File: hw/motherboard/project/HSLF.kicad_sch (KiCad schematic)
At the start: 41 parts, among them SW1 SW_Push, SW2 SW_Push, U1 STM32F103C8T6, U2 TPS563201, U3 AMS1117-5.0, Y1 12MHz, Y2 DNP 32.768k

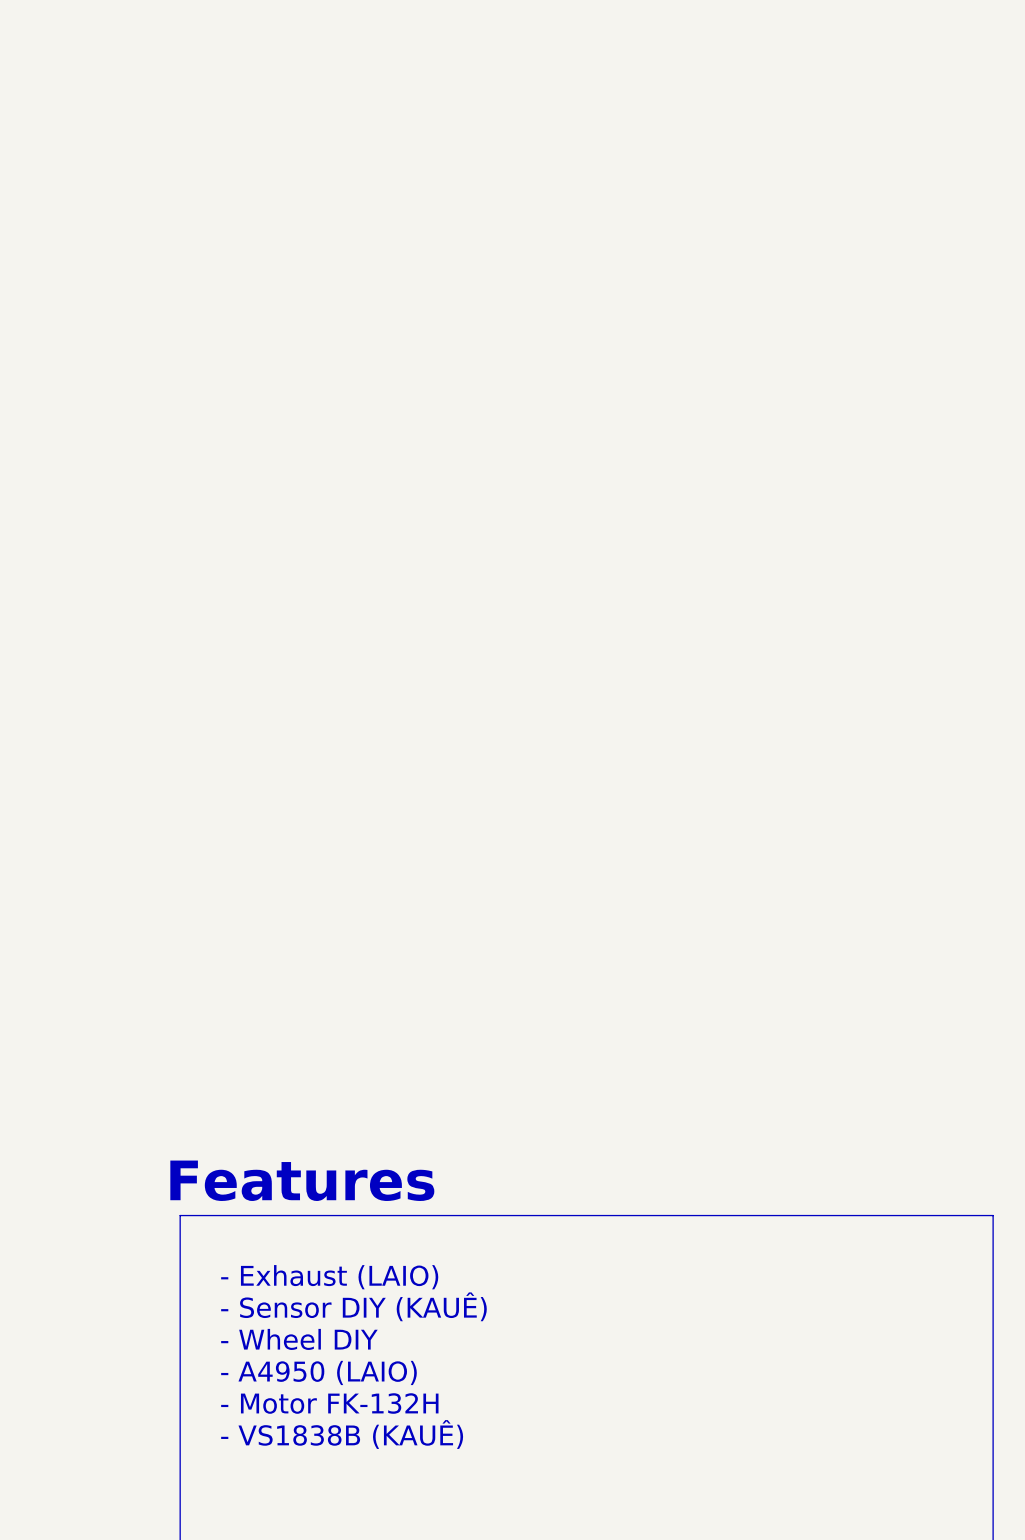
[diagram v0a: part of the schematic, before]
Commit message: Add Features and Sugestions, add sensors-array project
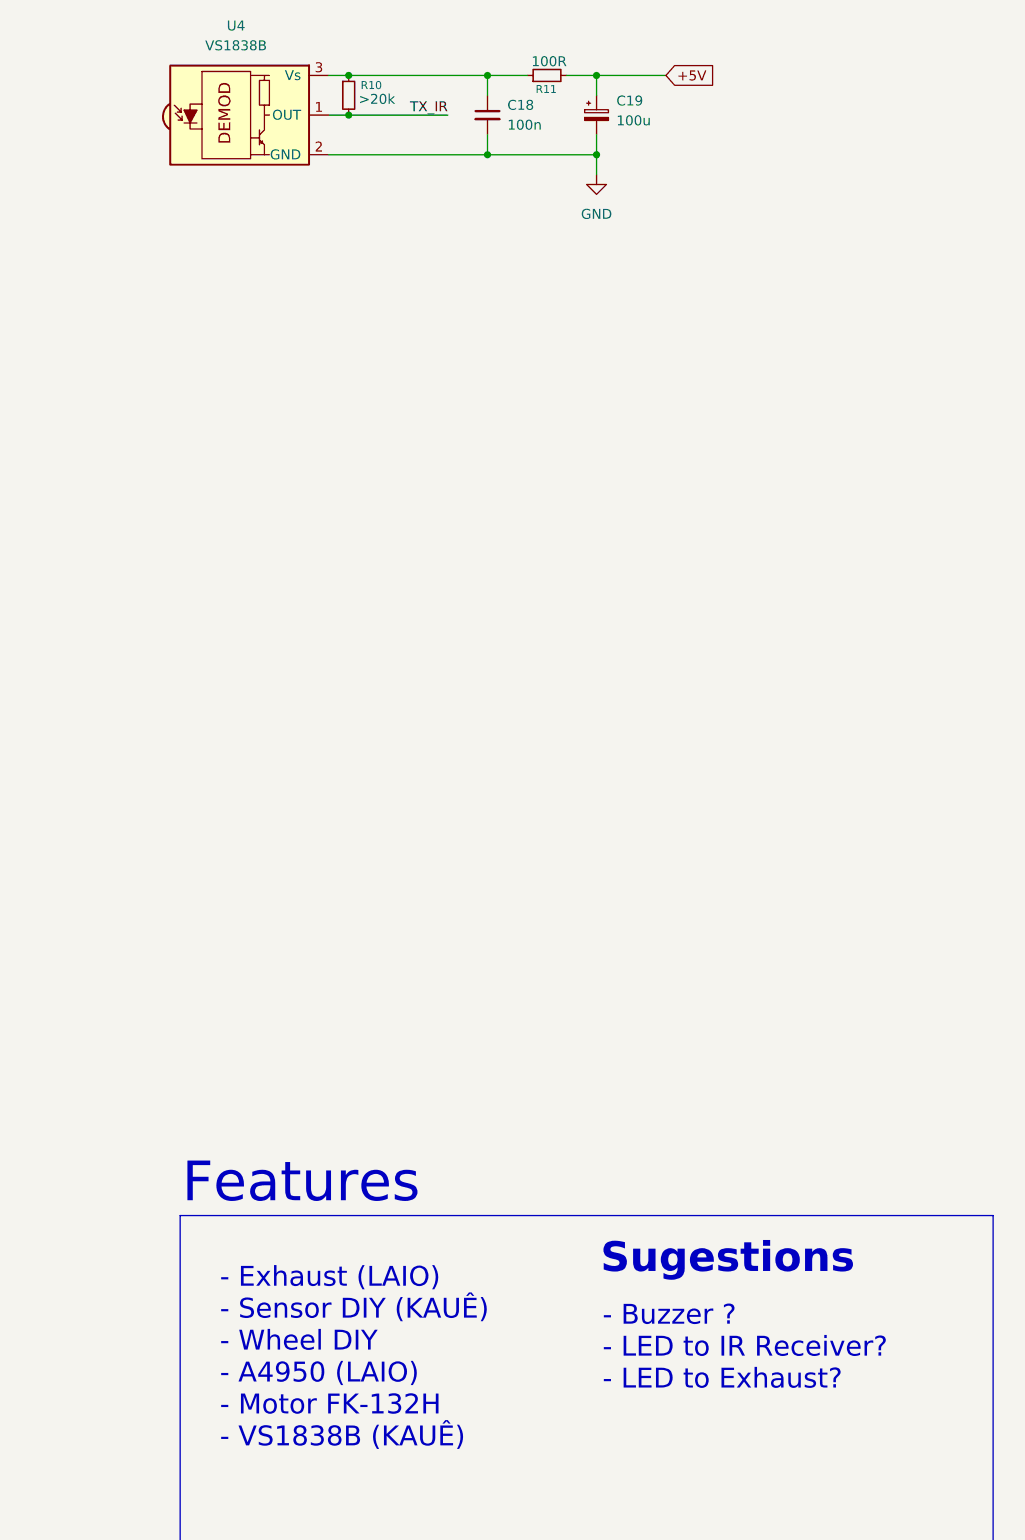
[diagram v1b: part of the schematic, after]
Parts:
- added C18: 100n, symbol Device:C_Small
- added C19: 100u, symbol Device:C_Polarized_Small
- added R10: >20k, symbol Device:R_Small
- added R11: 100R, symbol Device:R_Small
- added U4: VS1838B, OptoDevice:Vishay_MOLD-3Pin, symbol Interface_Optical:TSDP341xx
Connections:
- net +5V: now also C19.1, R11.2
- net GND: now also C18.2, C19.2, U4.2 (GND)
- new net: C18.1, R10.1, R11.1, U4.3 (Vs)
- new net TX_IR: R10.2, U4.1 (OUT)
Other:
- note added: "- Buzzer ? - LED to IR Receiver? - LED to Exhaust?"
- note added: "Sugestions"

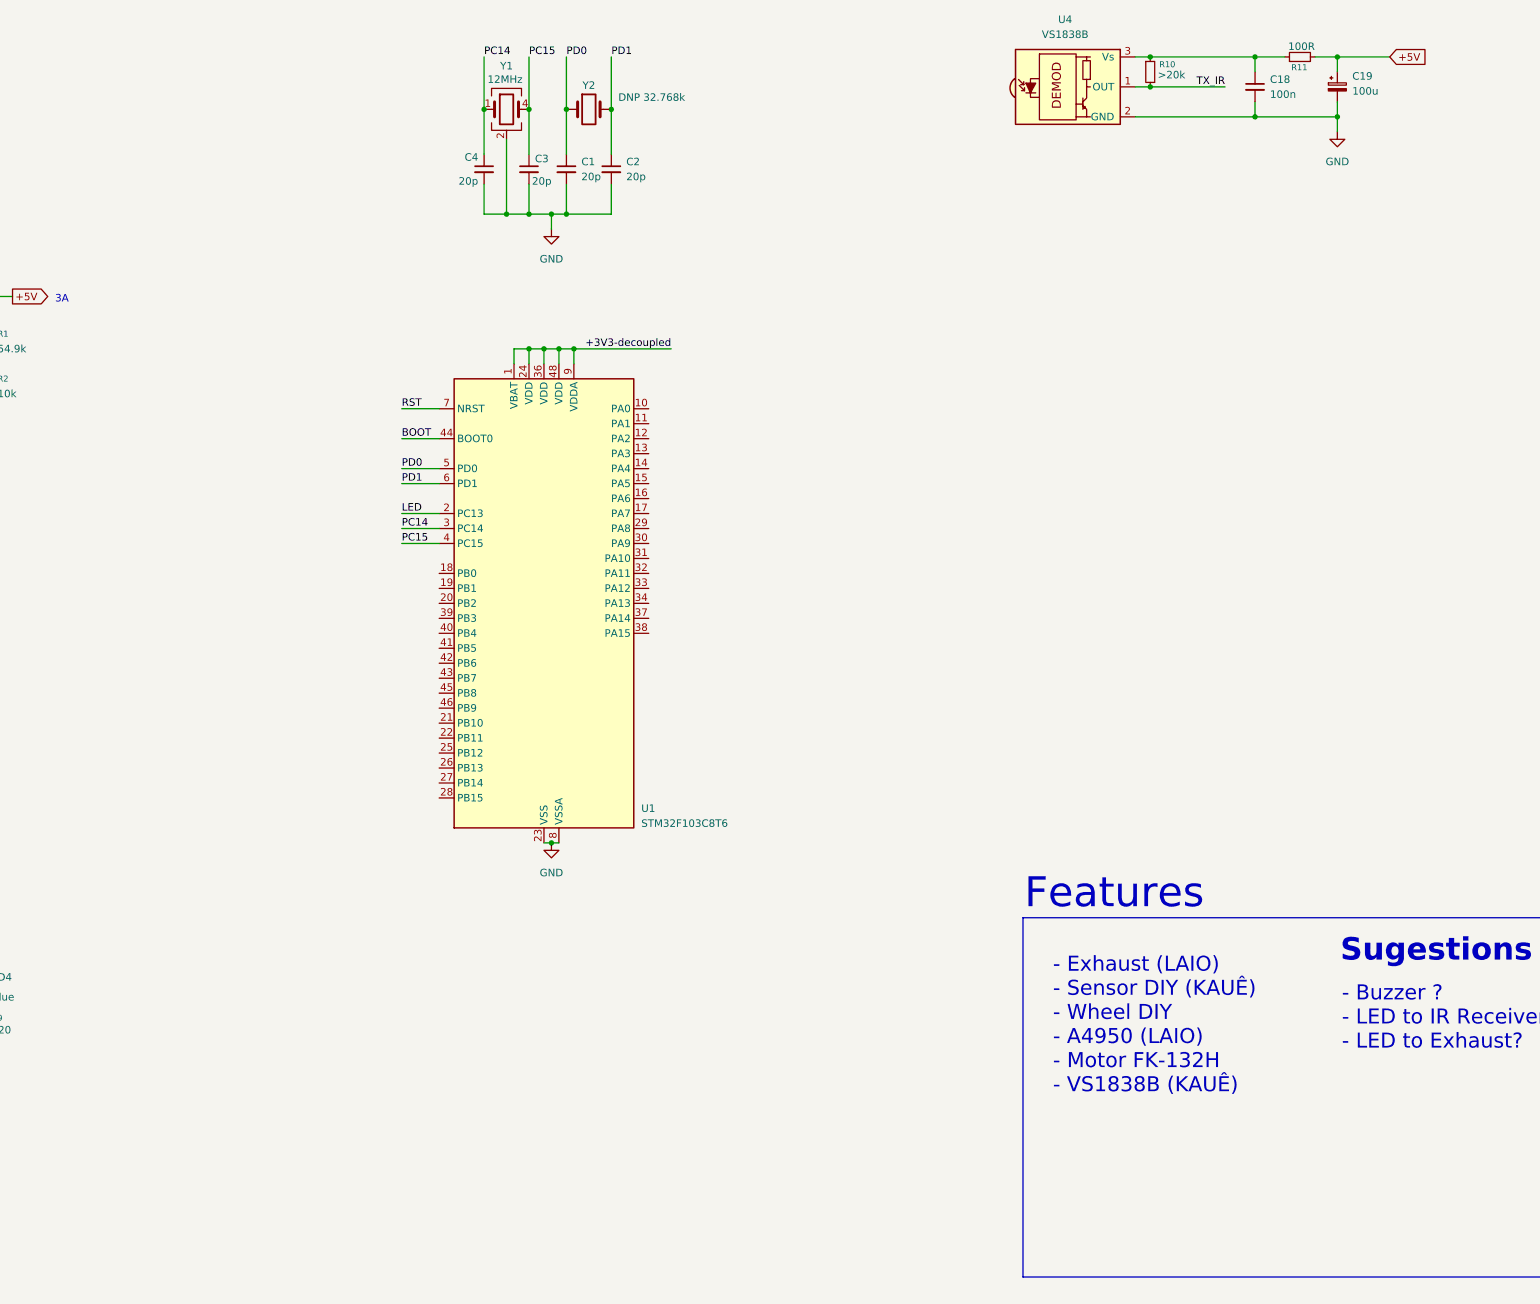
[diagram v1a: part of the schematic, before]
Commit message: criacao do driver do exaustor e driver para motores de tracao
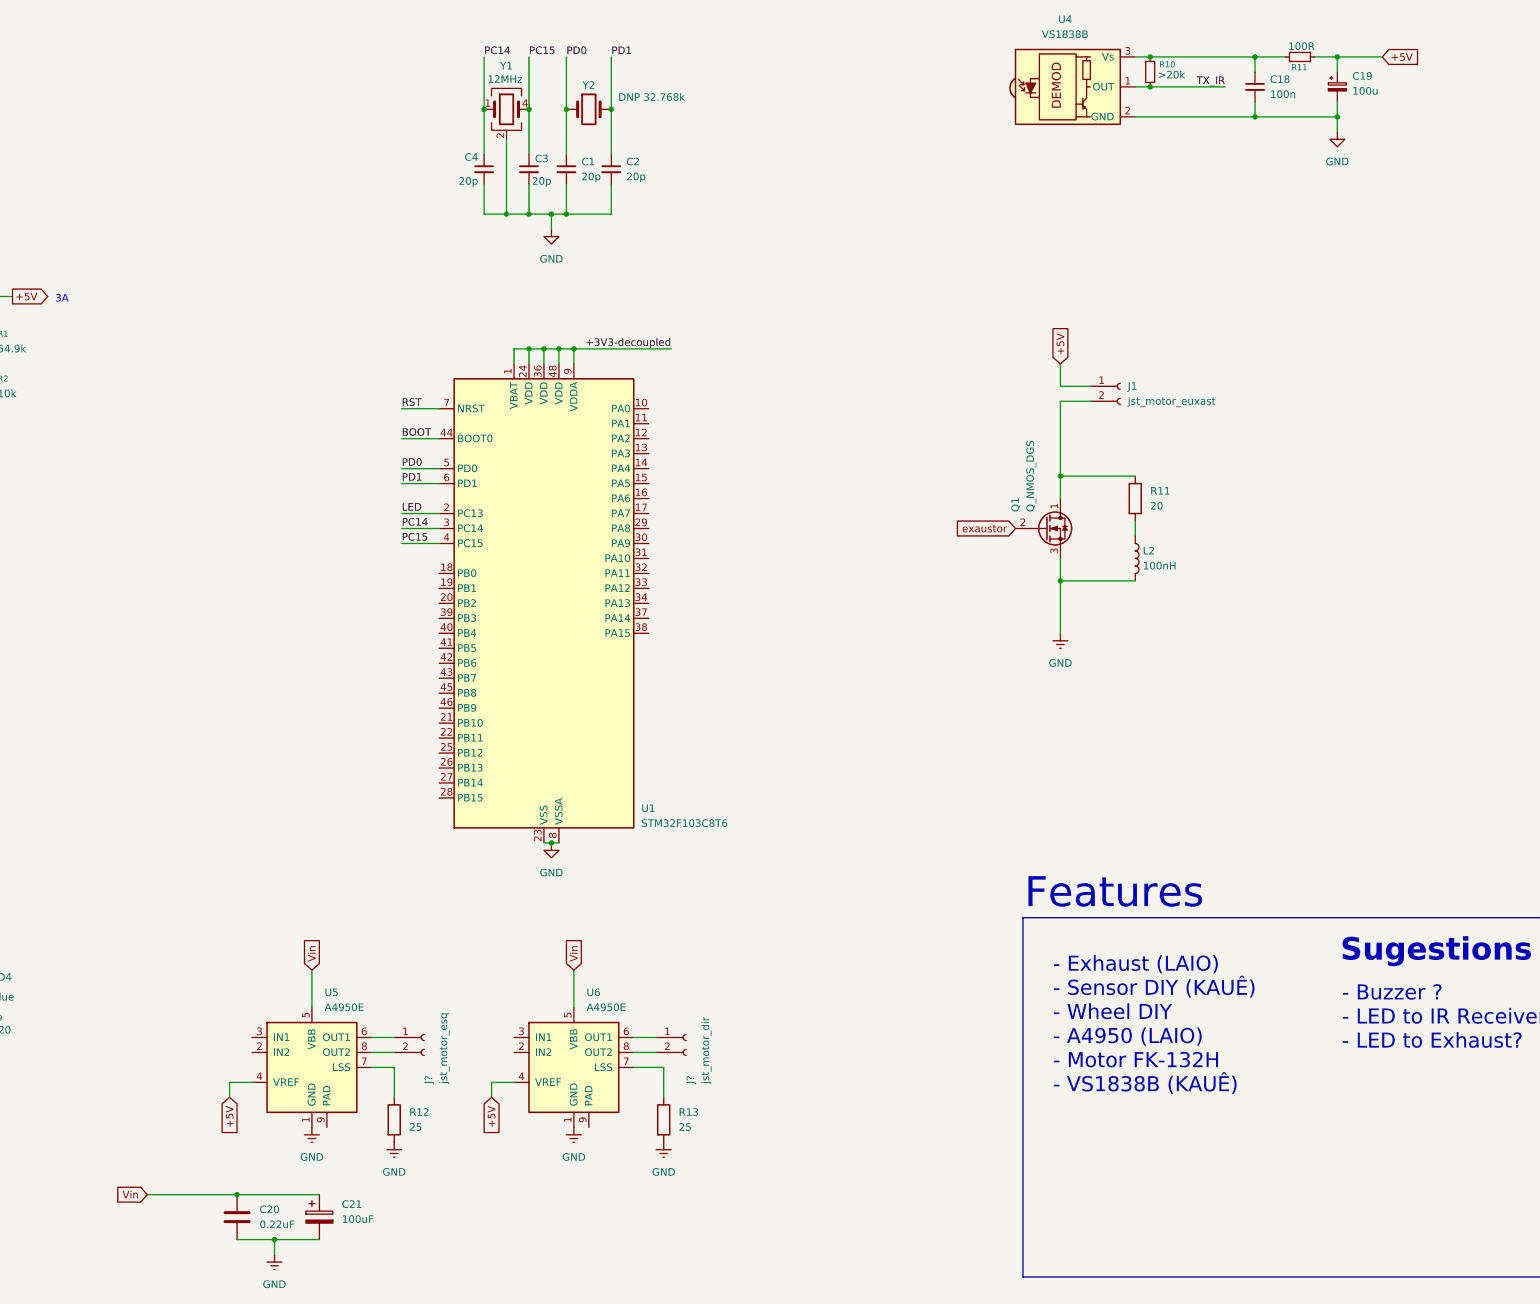
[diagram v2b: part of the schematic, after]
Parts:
- added C20: 0.22uF, symbol Device:C
- added C21: 100uF, symbol Device:C_Polarized
- added J1: jst_motor_euxast, symbol Connector:Conn_01x02_Socket
- added J?: jst_motor_esq, symbol Connector:Conn_01x02_Socket
- added J?: jst_motor_dir, symbol Connector:Conn_01x02_Socket
- added L2: 100nH, symbol Device:L
- added Q1: Q_NMOS_DGS, symbol Transistor_FET:Q_NMOS_DGS
- added R11: 20, symbol Device:R
- added R12, R13: 25, symbol Device:R
- added U5, U6: A4950E, Package_SO:SOIC-8-1EP_3.9x4.9mm_P1.27mm_EP2.41x3.3mm, symbol Driver_Motor:A4950E
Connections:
- net +5V: now also J1.1 (Pin_1), U5.4 (VREF), U6.4 (VREF)
- net GND: now also C20.2, C21.2, L2.2, Q1.3 (S), R12.2, R13.2, U5.1 (GND), U6.1 (GND)
- net Vin: now also C20.1, C21.1, U5.5 (VBB), U6.5 (VBB)
- new net: R13.1, U6.7 (LSS)
- new net: J?.1 (Pin_1), U6.6 (OUT1)
- new net: J?.2 (Pin_2), U6.8 (OUT2)
- new net: J?.1 (Pin_1), U5.6 (OUT1)
- new net: J?.2 (Pin_2), U5.8 (OUT2)
- new net: J1.2 (Pin_2), Q1.1 (D), R11.1
- new net: L2.1, R11.2
- new net: R12.1, U5.7 (LSS)
- new net exaustor: Q1.2 (G)

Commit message: finalizacao dodriver do propucao do carro
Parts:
- added R14: 10k, symbol Device:R_Small
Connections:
- net GND: now also R14.2
- net exaustor: now also U1.31 (PA10), R14.1
- net MOTOR_DIR2: now reaches U6.2 (IN2)
- net MOTOR_DIR2: now also U1.46 (PB9)
- net MOTOR_DIR1: now reaches U6.3 (IN1)
- net MOTOR_DIR1: now also U1.45 (PB8)
- net MOTOR_ESQ1: now reaches U1.42 (PB6)
- net MOTOR_ESQ1: now also U5.3 (IN1)
- net MOTOR_ESQ2: now reaches U1.43 (PB7)
- net MOTOR_ESQ2: now also U5.2 (IN2)
- no-connect marks 0 -> 2
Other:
- moved on the sheet: C20, C21

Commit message: finalizacao dodriver do propucao do carro
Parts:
- removed L2: 100nH, symbol Device:L
- added C22: 100nF, symbol Device:C
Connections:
- net GND: now also C22.2
- net at R11.2: now also C22.1
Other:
- note added: "- Buzzer NO - LED to Exhaust YES"
- note removed: "- Buzzer ? - LED to IR Receiver? - LED to Exhaust?"
- moved on the sheet: C20, C21, J?, R12, R13, U5, U6

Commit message: Add the jst connector for sensors-arrays and modify to jst conn for all connectors
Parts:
- removed J1: jst_motor_euxast, symbol Connector:Conn_01x02_Socket
- removed J?: jst_motor_esq, symbol Connector:Conn_01x02_Socket
- removed J?: jst_motor_dir, symbol Connector:Conn_01x02_Socket
- added C23, C24: 100u, symbol Device:C_Polarized_Small
- added C25: 100n, symbol Device:C_Small
- added D5: RED, symbol Device:LED
- added J1, J3, J4: JST_01x02_Pin, symbol Connector:Conn_01x02_Pin
- added J2: JST_01x14_Pin, symbol Connector:Conn_01x14_Pin
- added R15: 220, symbol Device:R_Small
- R11, R7: value 100R -> 100
- R8: value 220R -> 220
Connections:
- net +3V3: now also C23.1; no longer U1.9 (VDDA)
- net +5V: now also U1.9 (VDDA), C24.1, C25.1, J1.2 (Pin_2), J2.1 (Pin_1)
- net GND: now also C23.2, C24.2, C25.2, J2.14 (Pin_14), R15.2
- net exaustor: now also D5.2 (A)
- net at U6.6 (OUT1): now also J3.2 (Pin_2)
- net at U6.8 (OUT2): now also J3.1 (Pin_1)
- net at U5.6 (OUT1): now also J4.2 (Pin_2)
- net at U5.8 (OUT2): now also J4.1 (Pin_1)
- net at Q1.1 (D), R11.1: now also J1.1 (Pin_1)
- new net: D5.1 (K), R15.1
- new net A0: J2.2 (Pin_2)
- new net A1: J2.3 (Pin_3)
- new net A10: J2.12 (Pin_12)
- new net A11: J2.13 (Pin_13)
- new net A2: J2.4 (Pin_4)
- new net A3: J2.5 (Pin_5)
- new net A4: J2.6 (Pin_6)
- new net A5: J2.7 (Pin_7)
- new net A6: J2.8 (Pin_8)
- new net A7: J2.9 (Pin_9)
- new net A8: J2.10 (Pin_10)
- new net A9: J2.11 (Pin_11)

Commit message: finalize the motherboard schematic v0
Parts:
- removed C1, C2: 20p, symbol Device:C_Small
- removed C23: 100u, symbol Device:C_Polarized_Small
- removed D1: D_Schottky_Small_Filled, symbol Device:D_Schottky_Small_Filled
- removed J2: JST_01x14_Pin, symbol Connector:Conn_01x14_Pin
- removed Y1: 12MHz, symbol Device:Crystal_GND23
- removed Y2: DNP 32.768k, symbol Device:Crystal
- added C23: 1u, symbol Device:C_Small
- added C26: 100n, symbol Device:C_Small
- added D1: Power-ON, symbol Device:LED_Small
- added D6, D7: 1N5817, Diode_THT:D_DO-41_SOD81_P10.16mm_Horizontal, symbol Diode:1N5817
- added J2: Conn_01x12_Pin, symbol Connector:Conn_01x12_Pin
- added J5: IDC_Conn_STLink-V2, symbol Connector_Generic:Conn_02x05_Counter_Clockwise
- added J6: USB4940-00-A, USB494000A, symbol High_Speed_Line_Follower_V1:USB4940-00-A
- added J7: XT60-M, symbol Connector:Conn_01x02_Pin
- added Q2: AO3401A, Package_TO_SOT_SMD:SOT-23, symbol Transistor_FET:AO3401A
- added R16, R17: 5k1, symbol Device:R_Small
- added R18, R19: 22, symbol Device:R_Small
- added R20: 10k, symbol Device:R_Small
- added R21: 1k, symbol Device:R_Small
- added SW3: SW_SPDT, symbol Switch:SW_SPDT
- added Y1: 16MHz, symbol Device:Crystal_GND24_Small
- C11, C14: value 0.1u -> 0u1
- C3, C4: value 20p -> 10p
- D5: value RED -> Exhaust-ON
- R1: value 54.9k -> 54k9
- R3: value 1,2k -> 1k2
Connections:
- net +3V3: now also C23.1, D7.2 (A), J5.4 (Pin_4), J5.7 (Pin_7)
- net A0: now also U1.10 (PA0), J2.2 (Pin_2)
- net A1: now also U1.11 (PA1), J2.3 (Pin_3)
- net A2: now also U1.12 (PA2), J2.4 (Pin_4)
- net A3: now also U1.13 (PA3), J2.5 (Pin_5)
- net A4: now also U1.14 (PA4), J2.6 (Pin_6)
- net A5: now also U1.15 (PA5), J2.7 (Pin_7)
- net A6: now also U1.16 (PA6), J2.8 (Pin_8)
- net A7: now also U1.17 (PA7), J2.9 (Pin_9)
- net A8: now also U1.18 (PB0), J2.10 (Pin_10)
- net A9: now also U1.19 (PB1), J2.11 (Pin_11)
- net GND: now also C23.2, C26.2, J2.12 (Pin_12), J5.2 (Pin_2), J5.9 (Pin_9), J6.A1 (GND_1), J6.B1 (GND_2), J6.S1 (GND_3), J6.S2 (GND_4), J6.S3 (GND_5), J6.S4 (GND_6), J7.2 (Pin_2), R16.1, R17.2, R20.1, R21.2, Y1.2 (G), Y1.4 (G)
- net RST: now also J5.1 (Pin_1)
- net TX_IR: now also U1.30 (PA9)
- net USBC_D-: now reaches U1.32 (PA11)
- net USBC_D-: now also J6.B7 (DN2), R19.2
- net USBC_D+: now reaches U1.33 (PA12)
- net USBC_D+: now also J6.B6 (DP2), R18.1
- net SWDIO: now reaches U1.34 (PA13)
- net SWDIO: now also J5.10 (Pin_10)
- net SWCLK: now reaches U1.37 (PA14)
- net SWCLK: now also J5.8 (Pin_8)
- net +5V renamed 5VA
- net 5VA: now also J2.1 (Pin_1), Q2.2 (S); no longer C16.1, D3.2 (A), U1.9 (VDDA), U3.3 (VI)
- net PC14: no longer names the net of U1.3 (PC14)
- net PC14: no longer C4.1
- net PC15: no longer names the net of U1.4 (PC15)
- net PC15: no longer C3.1
- net PD0 renamed HSE_IN
- net HSE_IN: now also C4.1, Y1.1
- net PD1 renamed HSE_OUT
- net HSE_OUT: now also C3.1, Y1.3
- net Vin renamed BATT
- net BATT: now also D1.2 (A), SW3.1 (A)
- new net: J7.1 (Pin_1), SW3.2 (B)
- new net: D1.1 (K), R21.1
- new net CC1: J6.A5 (CC1), R16.2
- new net CC2: J6.B5 (CC2), R17.1
- new net Conn_USBC_D+: J6.A6 (DP1), R18.2
- new net Conn_USBC_D-: J6.A7 (DN1), R19.1
- new net VBUS: D6.2 (A), J5.5 (Pin_5), J5.6 (Pin_6), J6.A4 (VBUS_1), J6.B4 (VBUS_2), Q2.1 (G), R20.2
- new net VDDA: C16.1, C26.1, D3.2 (A), D6.1 (K), D7.1 (K), Q2.3 (D), U1.9 (VDDA), U3.3 (VI)
- no-connect marks 2 -> 20
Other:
- note added: "Array-sensors connector"
- note added: "Automatic changeover switch"
- note added: "Debug LEDs"
- note added: "Exhaust"
- note added: "Hardware Reset and Boot Mode"
- note added: "IR Receiver"
- note added: "MCU"
- note added: "MCU Decoupling"
- note added: "Motor Drivers"
- note added: "Power Rails (5V/3V3)"
- note added: "Power Supply"
- note added: "USB type-C 2.0"
- company: Kauê Lucas Nascimento da Silva -> Kauê Lucas Nascimento da Silva & Laio
- moved on the sheet: C10, C11, C12, C13, C14, C15, C16, C17, C18, C19, C20, C21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
